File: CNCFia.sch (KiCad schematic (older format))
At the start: 23 parts, among them J1 GND, J10 Driver_X, J11 Driver_Y, J12 Driver_Z, J13 Coolant, J14 Spin_10V, J15 Spin_Enabl, J16 Spin_Dir, J17 Mist, J2 EXT_5V, J3 Limit SW_XY, J4 Limit SW_ZA, J5 Extra SW 0, J6 Extra SW 1, J7 EXT_12V, J8 OPTO_5V, J9 Signal Input, U6 24LC16

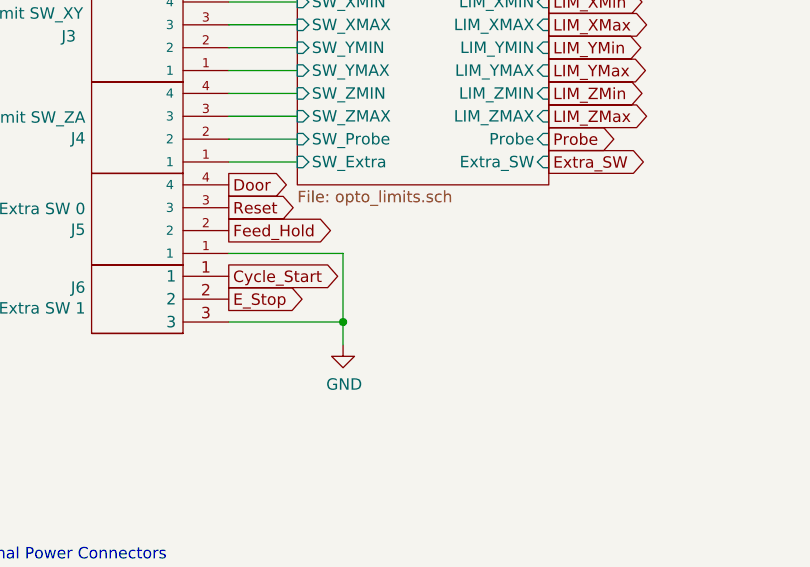
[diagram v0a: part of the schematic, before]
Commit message: Changed wrong GND for limit switches
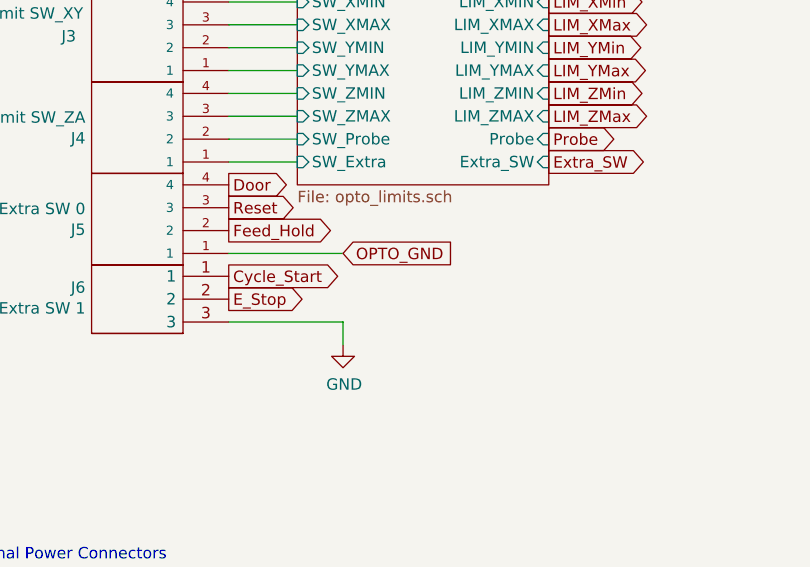
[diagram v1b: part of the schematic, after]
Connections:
- wire segments 86 -> 85
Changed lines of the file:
@@
 Comment9 ""
 $EndDescr
-Connection ~ 2450 3200
 Connection ~ 5400 4750
 Connection ~ 5400 5650
@@
 Wire Wire Line
 	2250 2400 1950 2400
-Wire Wire Line
-	2450 2900 2450 3200
 Wire Wire Line
 	9250 2150 8900 2150
@@
 Text GLabel 2000 5550 3    50   Output ~ 0
 EXT_5V
+Text GLabel 2450 2900 2    50   Input ~ 0
+OPTO_GND
 Text GLabel 3000 7100 2    50   Input ~ 0
 OPTO_GND

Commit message: Change mosfets and resistors to arrays
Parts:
- removed J6: Extra SW 1, Kicad_extra_components:CUI_TBP02R2-381-03BE, symbol SamacSys_Parts:TB008A-508-03BE
- added J6: Extra SW 0, Kicad_extra_components:CUI_TBP02R2-381-04BE, symbol TB008A-508-04BE:TB008A-508-04BE
- J1: value GND -> 5V_OUT
- J10, J11, J12: footprint Kicad_extra_components:CUI_TBP02R2-381-03BE -> Kicad_extra_components:CUI_TBP02R2-381-04BE; symbol SamacSys_Parts:TB008A-508-03BE -> TB008A-508-04BE:TB008A-508-04BE
- J2: value EXT_5V -> IN_EXT_5V
- J7: value EXT_12V -> IN_EXT_12V
- J8: value OPTO_5V -> IN_OPTO_PWR
- J9: footprint Connector_PinHeader_2.54mm:PinHeader_2x20_P2.54mm_Vertical -> Connector_PinHeader_2.54mm:PinHeader_2x16_P2.54mm_Vertical; symbol Connector_Generic:Conn_02x20_Odd_Even -> Connector_Generic:Conn_02x16_Odd_Even
- R5, R6: footprint Resistor_SMD:R_1206_3216Metric_Pad1.42x1.75mm_HandSolder -> Kicad_extra_components:R_0805_2012Metric_Pad1.15x1.40mm_HandSolder
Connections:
- wire segments 85 -> 118
- no-connect marks 11 -> 3
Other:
- moved on the sheet: J1, J13, J14, J15, J16, J17, J2, J3, J4, J5, J7, J8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

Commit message: Made it more neat and organized
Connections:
- wire segments 118 -> 119
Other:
- moved on the sheet: J14
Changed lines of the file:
@@
 	5300 4850 5300 4800
 Wire Wire Line
-	9050 2850 9050 2900
+	8950 2450 8950 2500
 Wire Wire Line
 	1000 4750 900  4750
@@
 	9000 1400 9100 1400
 Wire Wire Line
-	9050 2850 9150 2850
-Wire Wire Line
 	9100 1000 9000 1000
 Wire Wire Line
@@
 Wire Wire Line
 	6200 4400 6400 4400
+Wire Wire Line
+	8950 2450 9150 2450
+Wire Wire Line
+	9150 2450 9150 2650
 Wire Wire Line
 	1200 4900 1200 5150
@@
 L power:GND #PWR013
 U 1 1 5E35FECC
-P 9050 2900
-F 0 "#PWR013" H 9050 2650 50  0001 C CNN
-F 1 "GND" H 9055 2727 50  0000 C CNN
-F 2 "" H 9050 2900 50  0001 C CNN
-F 3 "" H 9050 2900 50  0001 C CNN
-	1    9050 2900
+P 8950 2500
+F 0 "#PWR013" H 8950 2250 50  0001 C CNN
+F 1 "GND" H 8955 2327 50  0000 C CNN
+F 2 "" H 8950 2500 50  0001 C CNN
+F 3 "" H 8950 2500 50  0001 C CNN
+	1    8950 2500
 	1    0    0    -1
 $EndComp
@@
 L SamacSys_Parts:TB008A-508-02BE J14
 U 1 1 5E91D3C1
-P 9150 2750
-F 0 "J14" H 9778 2746 50  0000 L CNN
-F 1 "Spin_10V" H 9778 2655 50  0000 L CNN
-F 2 "Kicad_extra_components:CUI_TBP02R2-381-02BE" H 9800 2850 50  0001 L CNN
-F 3 "https://componentsearchengine.com/Datasheets/1/TB008A-508-02BE.pdf" H 9800 2750 50  0001 L CNN
-F 4 "Fixed Terminal Blocks screw type, 5.08 , 45 , 2 poles, CUI Blue, slotted screw, PCB mount" H 9800 2650 50  0001 L CNN "Description"
-F 5 "15.82" H 9800 2550 50  0001 L CNN "Height"
-F 6 "490-TB008A-508-02BE" H 9800 2450 50  0001 L CNN "Mouser Part Number"
-F 7 "https://www.mouser.com/Search/Refine.aspx?Keyword=490-TB008A-508-02BE" H 9800 2350 50  0001 L CNN "Mouser Price/Stock"
-F 8 "CUI" H 9800 2250 50  0001 L CNN "Manufacturer_Name"
-F 9 "TB008A-508-02BE" H 9800 2150 50  0001 L CNN "Manufacturer_Part_Number"
-F 10 "102-6422-ND" H 9150 2750 50  0001 C CNN "Digi-Key_PN"
-F 11 "  	TBP01R2-508-02BE " H 9150 2750 50  0001 C CNN "MPN"
-F 12 "production" H 9150 2750 50  0001 C CNN "fit_field"
-F 13 "production" H 9150 2750 50  0001 C CNN "Config"
-	1    9150 2750
+P 9150 2650
+F 0 "J14" H 9778 2646 50  0000 L CNN
+F 1 "Spin_10V" H 9778 2555 50  0000 L CNN
+F 2 "Kicad_extra_components:CUI_TBP02R2-381-02BE" H 9800 2750 50  0001 L CNN
+F 3 "https://componentsearchengine.com/Datasheets/1/TB008A-508-02BE.pdf" H 9800 2650 50  0001 L CNN
+F 4 "Fixed Terminal Blocks screw type, 5.08 , 45 , 2 poles, CUI Blue, slotted screw, PCB mount" H 9800 2550 50  0001 L CNN "Description"
+F 5 "15.82" H 9800 2450 50  0001 L CNN "Height"
+F 6 "490-TB008A-508-02BE" H 9800 2350 50  0001 L CNN "Mouser Part Number"
+F 7 "https://www.mouser.com/Search/Refine.aspx?Keyword=490-TB008A-508-02BE" H 9800 2250 50  0001 L CNN "Mouser Price/Stock"
+F 8 "CUI" H 9800 2150 50  0001 L CNN "Manufacturer_Name"
+F 9 "TB008A-508-02BE" H 9800 2050 50  0001 L CNN "Manufacturer_Part_Number"
+F 10 "102-6422-ND" H 9150 2650 50  0001 C CNN "Digi-Key_PN"
+F 11 "  	TBP01R2-508-02BE " H 9150 2650 50  0001 C CNN "MPN"
+F 12 "production" H 9150 2650 50  0001 C CNN "fit_field"
+F 13 "production" H 9150 2650 50  0001 C CNN "Config"
+	1    9150 2650
 	1    0    0    -1
 $EndComp
@@
 F13 "Relay_NC_3" I R 8750 4250 50
 F14 "Relay_In_4" I L 7450 3850 50
-F15 "Relay_COM_4" I R 8750 4600 50
-F16 "Relay_NO_4" I R 8750 4700 50
-F17 "Relay_NC_4" I R 8750 4800 50
+F15 "Relay_COM_4" I R 8750 4700 50
+F16 "Relay_NO_4" I R 8750 4800 50
+F17 "Relay_NC_4" I R 8750 4600 50
 $EndSheet
 $Sheet

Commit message: Fixing Symbols
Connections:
- net labels added: +3V3
- net labels removed: +3.3V

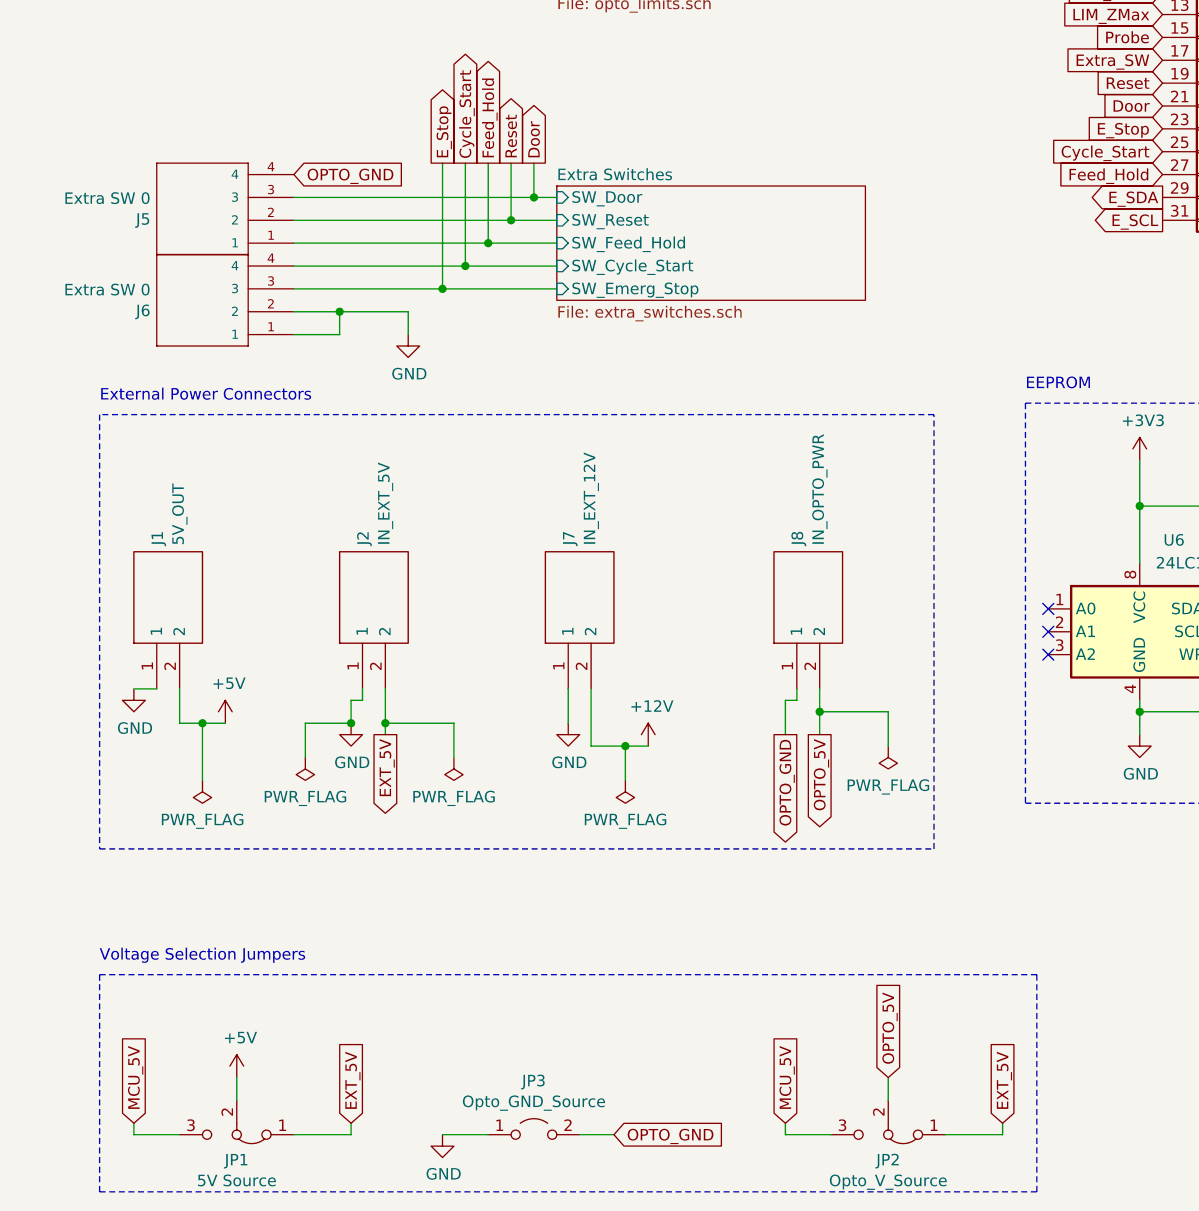
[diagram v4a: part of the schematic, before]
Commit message: Simplify the power options
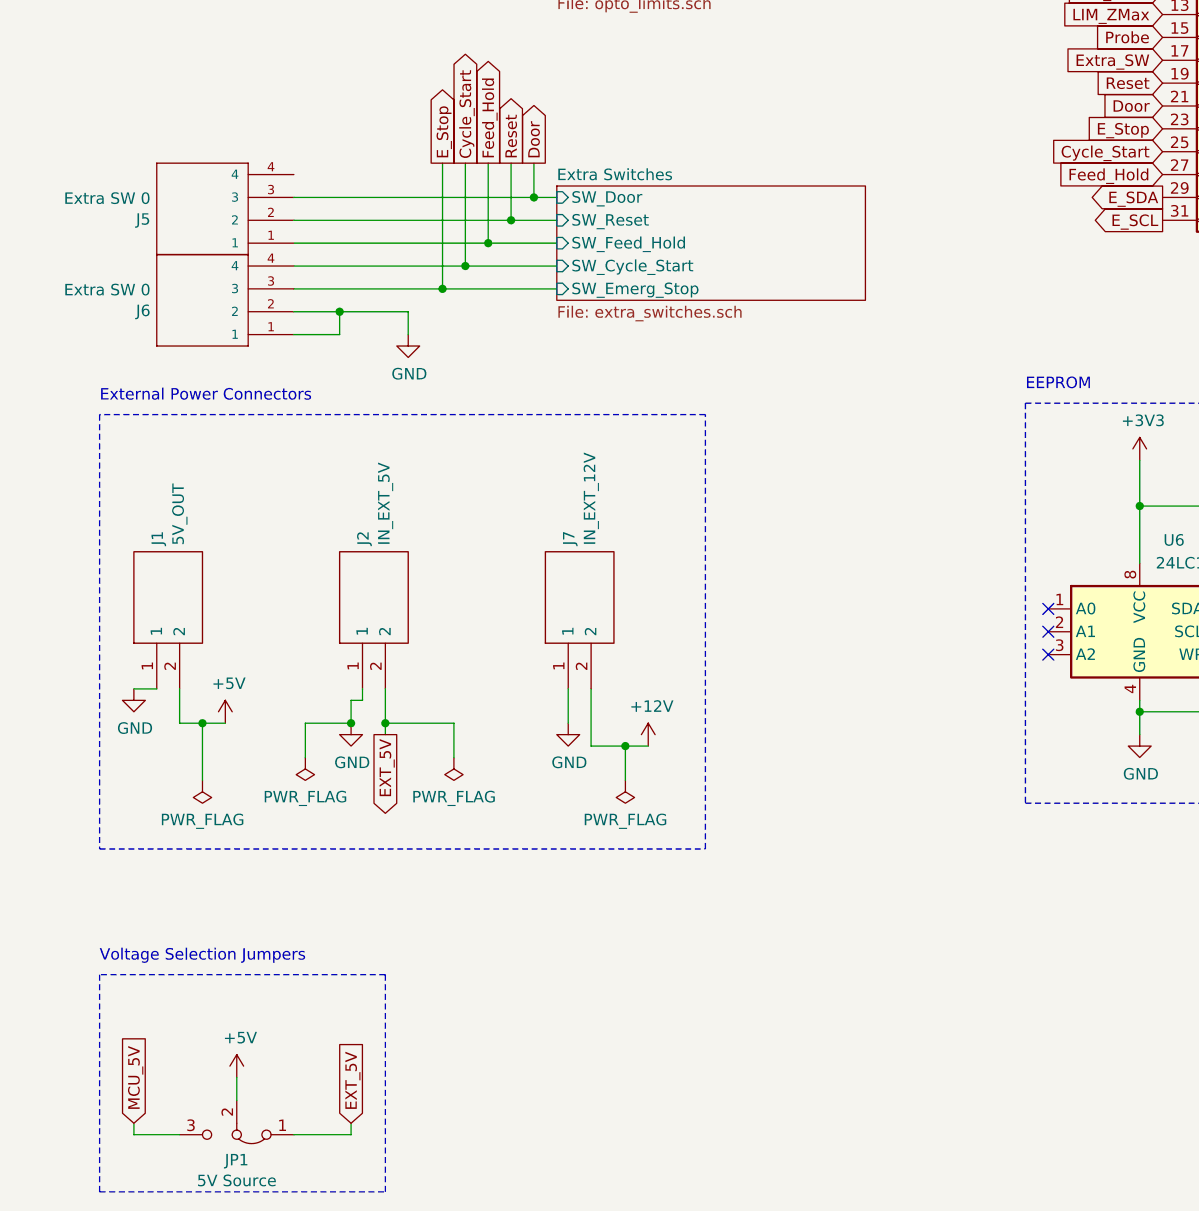
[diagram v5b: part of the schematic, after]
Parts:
- removed J8: IN_OPTO_PWR, Kicad_extra_components:CUI_TBP02R2-381-02BE, symbol SamacSys_Parts:TB008A-508-02BE
- removed JP2: Opto_V_Source, Connector_PinHeader_2.54mm:PinHeader_1x03_P2.54mm_Vertical, symbol Jumper:Jumper_3_Bridged12
- removed JP3: Opto_GND_Source, Connector_PinHeader_2.54mm:PinHeader_1x02_P2.54mm_Vertical, symbol Jumper:Jumper_2_Open
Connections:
- net OPTO_GND: no longer names the net of J5.4
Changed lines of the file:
@@
 Connection ~ 2650 2600
 Connection ~ 3050 5000
-Connection ~ 3900 4850
 Connection ~ 5300 3950
 Connection ~ 5300 4850
@@
 	2450 2800 2750 2800
 Wire Wire Line
-	2450 6700 2250 6700
-Wire Wire Line
 	2550 2450 2550 2700
 Wire Wire Line
@@
 	2800 4900 2800 4750
 Wire Wire Line
-	2850 6700 3000 6700
-Wire Wire Line
 	2900 4750 2900 5000
 Wire Wire Line
@@
 	3050 5000 3150 5000
 Wire Wire Line
-	3750 4800 3750 4950
-Wire Wire Line
-	3750 6700 3750 6650
-Wire Wire Line
-	3800 4750 3800 4800
-Wire Wire Line
-	3800 4800 3750 4800
-Wire Wire Line
-	3900 4750 3900 4850
-Wire Wire Line
-	3900 4850 3900 4950
-Wire Wire Line
-	3900 4850 4200 4850
-Wire Wire Line
-	3950 6700 3750 6700
-Wire Wire Line
-	4200 4850 4200 5000
-Wire Wire Line
-	4200 6450 4200 6550
-Wire Wire Line
-	4450 6700 4700 6700
-Wire Wire Line
-	4700 6650 4700 6700
-Wire Wire Line
 	4800 1050 5250 1050
 Wire Wire Line
@@
 	750  3550 750  5450
 Wire Notes Line
-	750  5450 4400 5450
+	750  5450 3400 5450
 Wire Notes Line
 	750  6000 750  6950
 Wire Notes Line
-	750  6950 4850 6950
-Wire Notes Line
-	4400 3550 750  3550
-Wire Notes Line
-	4400 5450 4400 3550
+	750  6950 2000 6950
+Wire Notes Line
+	2000 6000 750  6000
+Wire Notes Line
+	2000 6950 2000 6000
+Wire Notes Line
+	3400 3550 750  3550
+Wire Notes Line
+	3400 5450 3400 3550
 Wire Notes Line
 	4800 3500 4800 5250
@@
 Wire Notes Line
 	4800 5250 6800 5250
-Wire Notes Line
-	4850 6000 750  6000
-Wire Notes Line
-	4850 6950 4850 6000
 Wire Notes Line
 	6800 5250 6800 3500
@@
 Text GLabel 900  6650 1    50   Input ~ 0
 MCU_5V
-Text GLabel 1600 2500 2    50   Input ~ 0
-OPTO_GND
 Text GLabel 1850 6650 1    50   Input ~ 0
 EXT_5V
@@
 Text GLabel 2650 2450 1    50   Output ~ 0
 Door
-Text GLabel 3000 6700 2    50   Input ~ 0
-OPTO_GND
-Text GLabel 3750 4950 3    50   Output ~ 0
-OPTO_GND
-Text GLabel 3750 6650 1    50   Input ~ 0
-MCU_5V
-Text GLabel 3900 4950 3    50   Output ~ 0
-OPTO_5V
 Text GLabel 4100 900  2    50   Output ~ 0
 LIM_XMin
@@
 Text GLabel 4100 1600 2    50   Output ~ 0
 Extra_SW
-Text GLabel 4200 6450 1    50   Input ~ 0
-OPTO_5V
-Text GLabel 4700 6650 1    50   Input ~ 0
-EXT_5V
 Text GLabel 5400 1300 0    50   Input ~ 0
 LIM_XMin
@@
 $EndComp
 $Comp
-L power:PWR_FLAG #FLG0104
-U 1 1 5E767917
-P 4200 5000
-F 0 "#FLG0104" H 4200 5075 50  0001 C CNN
-F 1 "PWR_FLAG" H 4200 5173 50  0000 C CNN
-F 2 "" H 4200 5000 50  0001 C CNN
-F 3 "~" H 4200 5000 50  0001 C CNN
-	1    4200 5000
-	-1   0    0    1
-$EndComp
-$Comp
 L power:PWR_FLAG #FLG0106
 U 1 1 5E76F202
@@
 $EndComp
 $Comp
-L power:GND #PWR08
-U 1 1 5E8C0CA2
-P 2250 6700
-F 0 "#PWR08" H 2250 6450 50  0001 C CNN
-F 1 "GND" H 2255 6527 50  0000 C CNN
-F 2 "" H 2250 6700 50  0001 C CNN
-F 3 "" H 2250 6700 50  0001 C CNN
-	1    2250 6700
-	1    0    0    -1
-$EndComp
-$Comp
 L power:GND #PWR06
 U 1 1 5E306D9B
@@
 F 5 "CRGCQ1206F2K2" H 6200 4100 50  0001 C CNN "MPN"
 	1    6200 4100
-	1    0    0    -1
-$EndComp
-$Comp
-L Jumper:Jumper_2_Open JP3
-U 1 1 5E8CC50A
-P 2650 6700
-F 0 "JP3" H 2650 6935 50  0000 C CNN
-F 1 "Opto_GND_Source" H 2650 6844 50  0000 C CNN
-F 2 "Connector_PinHeader_2.54mm:PinHeader_1x02_P2.54mm_Vertical" H 2650 6700 50  0001 C CNN
-F 3 "~" H 2650 6700 50  0001 C CNN
-F 4 "production" H 2650 6700 50  0001 C CNN "fit_field"
-F 5 "production" H 2650 6700 50  0001 C CNN "Config"
-	1    2650 6700
 	1    0    0    -1
 $EndComp
@@
 F 5 "production" H 1350 6700 50  0001 C CNN "Config"
 	1    1350 6700
-	-1   0    0    1
-$EndComp
-$Comp
-L Jumper:Jumper_3_Bridged12 JP2
-U 1 1 5E8E9F02
-P 4200 6700
-F 0 "JP2" H 4200 6811 50  0000 C CNN
-F 1 "Opto_V_Source" H 4200 6902 50  0000 C CNN
-F 2 "Connector_PinHeader_2.54mm:PinHeader_1x03_P2.54mm_Vertical" H 4200 6700 50  0001 C CNN
-F 3 "~" H 4200 6700 50  0001 C CNN
-F 4 "production" H 4200 6700 50  0001 C CNN "fit_field"
-F 5 "production" H 4200 6700 50  0001 C CNN "Config"
-	1    4200 6700
 	-1   0    0    1
 $EndComp
@@
 	0    -1   -1   0
 $EndComp
-$Comp
-L SamacSys_Parts:TB008A-508-02BE J8
-U 1 1 5E87F045
-P 3800 4750
-F 0 "J8" H 4428 4746 50  0000 L CNN
-F 1 "IN_OPTO_PWR" H 4428 4655 50  0000 L CNN
-F 2 "Kicad_extra_components:CUI_TBP02R2-381-02BE" H 4450 4850 50  0001 L CNN
-F 3 "https://componentsearchengine.com/Datasheets/1/TB008A-508-02BE.pdf" H 4450 4750 50  0001 L CNN
-F 4 "Fixed Terminal Blocks screw type, 5.08 , 45 , 2 poles, CUI Blue, slotted screw, PCB mount" H 4450 4650 50  0001 L CNN "Description"
-F 5 "15.82" H 4450 4550 50  0001 L CNN "Height"
-F 6 "490-TB008A-508-02BE" H 4450 4450 50  0001 L CNN "Mouser Part Number"
-F 7 "https://www.mouser.com/Search/Refine.aspx?Keyword=490-TB008A-508-02BE" H 4450 4350 50  0001 L CNN "Mouser Price/Stock"
-F 8 "CUI" H 4450 4250 50  0001 L CNN "Manufacturer_Name"
-F 9 "TB008A-508-02BE" H 4450 4150 50  0001 L CNN "Manufacturer_Part_Number"
-F 10 "102-6422-ND" H 3800 4750 50  0001 C CNN "Digi-Key_PN"
-F 11 "  	TBP01R2-508-02BE " H 3800 4750 50  0001 C CNN "MPN"
-F 12 "production" H 3800 4750 50  0001 C CNN "fit_field"
-F 13 "production" H 3800 4750 50  0001 C CNN "Config"
-	1    3800 4750
-	0    -1   -1   0
-$EndComp

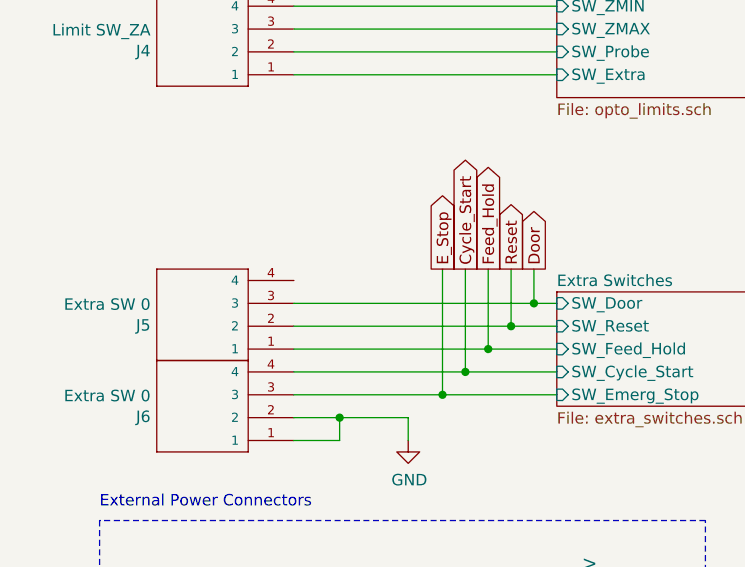
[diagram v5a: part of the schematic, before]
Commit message: Simplify the power options again
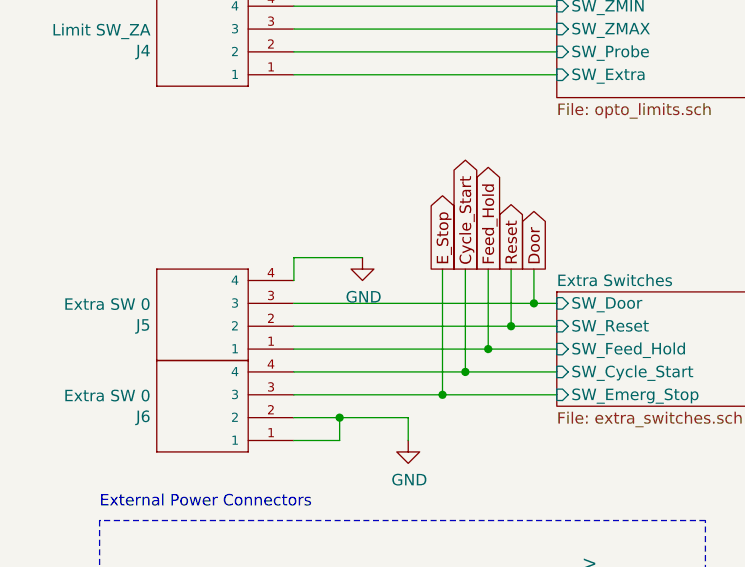
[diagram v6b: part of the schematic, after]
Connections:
- net GND: now also J5.4
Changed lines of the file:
@@
 	1600 1600 2750 1600
 Wire Wire Line
+	1600 2400 1600 2500
+Wire Wire Line
 	1600 2600 2650 2600
 Wire Wire Line
@@
 Wire Wire Line
 	1850 6650 1850 6700
+Wire Wire Line
+	1900 2400 1600 2400
 Wire Wire Line
 	1900 4750 1900 4800
@@
 	1    0    0    -1
 $EndComp
+$Comp
+L power:GND #PWR?
+U 1 1 5E496D8C
+P 1900 2400
+F 0 "#PWR?" H 1900 2150 50  0001 C CNN
+F 1 "GND" H 1905 2227 50  0000 C CNN
+F 2 "" H 1900 2400 50  0001 C CNN
+F 3 "" H 1900 2400 50  0001 C CNN
+	1    1900 2400
+	1    0    0    -1
+$EndComp
